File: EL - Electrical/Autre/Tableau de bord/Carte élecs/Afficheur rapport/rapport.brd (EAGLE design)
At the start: 54.9 x 40.9 mm, 15 parts, among them IC1 MCP23008P, X1 22-23-2041

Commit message: Afficheur rapport maj
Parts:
- moved R6 16.1 mm to (44.1, 12.7)
- moved R5 12.4 mm to (29.2, 0.32)
- moved R8 7.63 mm to (28.6, 12.7)
- moved R9 7.31 mm to (28.6, 9.84)
- moved R3 2.56 mm to (28.6, 15.2)
- moved R4 2.56 mm to (28.6, 17.8)
- moved R7 1.42 mm to (29.5, 6.99)
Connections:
- net N$8 renamed SCL
- net N$9 renamed SDA
- removed net N$1: IC1.16, R3.2
- removed net N$3: IC1.14, R5.2
- removed net N$4: IC1.13, R6.2
- removed net N$6: IC1.11, R8.2
- removed net N$7: IC1.10, R9.2
- new net GP0: IC1.10, R5.2
- new net GP1: IC1.11
- new net GP2: IC1.12
- new net GP3: IC1.13, R7.2
- new net GP4: IC1.14, R8.2
- new net GP5: IC1.15, R3.2
- new net GP6: IC1.16, R4.2
- net GND: now also LED1.5
- net N$2: now also R9.2; no longer IC1.15, R4.2
- net N$5: now also R6.2; no longer IC1.12, R7.2
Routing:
- net GND: track 53.6 -> 79.6 mm
- net N$11: track 37.9 -> 30.1 mm
- net N$10: track 49.1 -> 42.2 mm
- net N$14: track 11.9 -> 7.60 mm
- net N$12: track 21.3 -> 17.2 mm
- net N$13: track 14.7 -> 10.6 mm
- net N$16: track 19.5 -> 22.2 mm
- net N$3: track 2.36 -> 0.00 mm
- net N$6: track 2.36 -> 0.00 mm
- net N$4: track 2.27 -> 0.00 mm
- net N$7: track 2.27 -> 0.00 mm
- net N$1: track 2.27 -> 0.00 mm
- net N$5: track 2.22 -> 0.00 mm
- net N$2: track 2.22 -> 0.00 mm
- net N$15: track 21.0 -> 19.3 mm

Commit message: carte afficheur rapport et commandes
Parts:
- removed R3, R4, R5, R6, R7, R8, R9: 470, rcl:0204/7
- added RA, RB, RC, RD, RE, RF, RG: 470, rcl:0204/7
- moved R1 12.8 mm to (23.5, 25.7)
- moved C3 11.4 mm to (6.67, 24.1), turned to 90 degrees
- moved X1 10.3 mm to (23.5, 31.4), turned to 180 degrees
- moved C2 9.89 mm to (13.7, 30.2), turned to 90 degrees
- moved R2 7.31 mm to (6.67, 16.2), turned to 90 degrees
- moved IC1 2.86 mm to (15.6, 12.7)
- moved LED1 2.56 mm to (44.1, 19.4)
- moved C1 1.62 mm to (6.67, 6.67), turned to 270 degrees
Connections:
- removed net N$2: R9.2
- removed net N$5: R6.2
- net +5V: now also LED1.5, X1.1; no longer X1.2
- net GND: now also X1.4; no longer LED1.5, X1.1
- net GP0: now also RC.2; no longer R5.2
- net GP1: now also RD.2
- net GP2: now also RE.2
- net GP3: now also RG.2; no longer R7.2
- net GP4: now also RF.2; no longer R8.2
- net GP5: now also RA.2; no longer R3.2
- net GP6: now also RB.2; no longer R4.2
- net N$10: now also RG.1; no longer R9.1
- net N$11: now also RF.1; no longer R8.1
- net N$12: now also RE.1; no longer R7.1
- net N$13: now also RD.1; no longer R6.1
- net N$14: now also RC.1; no longer R5.1
- net N$15: now also RB.1; no longer R4.1
- net N$16: now also RA.1; no longer R3.1
- net SCL: now also X1.2; no longer X1.4
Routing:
- net GND: track 79.6 -> 53.8 mm
- net +5V: track 114.5 -> 99.7 mm
- net N$13: track 10.6 -> 18.3 mm
- net N$10: track 42.2 -> 36.4 mm
- net N$14: track 7.60 -> 12.8 mm
- net N$12: track 17.2 -> 21.7 mm
- net N$16: track 22.2 -> 26.6 mm
- net SCL: track 31.4 -> 27.7 mm
- net SDA: track 29.1 -> 25.7 mm
- net N$15: track 19.3 -> 21.9 mm
- net GP6: track 0.00 -> 2.54 mm
- net GP5: track 0.00 -> 2.54 mm
- net GP4: track 0.00 -> 2.54 mm
- net GP3: track 0.00 -> 2.54 mm
- net GP2: track 0.00 -> 2.54 mm
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- added copper zone on layer 1, net GND
- added copper zone on layer 1, net SDA
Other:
- board size 54.9 x 40.9 mm -> 63.5 x 38.1 mm
- board text added: "Afficheur Rapport Optimus V1.0"
- board text added: "GND SDA SCL +5V"

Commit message: test sublime merge
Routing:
- net +5V: track 99.7 -> 98.4 mm
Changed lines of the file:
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@@
 <wire x1="2.54" y1="0" x2="0" y2="2.54" width="0.1524" layer="20" curve="-90"/>
 <hole x="5.08" y="1.905" drill="0.0762"/>
-<hole x="11.1125" y="35.8775" drill="0.0762"/>
+<hole x="13.6525" y="35.56" drill="0.0762"/>
 <hole x="60.6425" y="2.54" drill="0.0762"/>
 <wire x1="60.96" y1="0" x2="63.5" y2="2.54" width="0.1524" layer="20" curve="90"/>
@@
 <wire x1="56.515" y1="7.62" x2="56.515" y2="35.56" width="0.1524" layer="20"/>
 <wire x1="56.515" y1="35.56" x2="56.515" y2="36.195" width="0.1524" layer="20"/>
+<dimension x1="2.54" y1="0" x2="2.54" y2="38.1" x3="-8.89" y3="19.05" textsize="1.778" layer="48"/>
+<dimension x1="0" y1="35.56" x2="56.515" y2="35.56" x3="28.2575" y3="43.4975" textsize="1.778" layer="48"/>
+<dimension x1="0" y1="2.54" x2="63.5" y2="2.54" x3="31.75" y3="-8.255" textsize="1.778" layer="48"/>
+<dimension x1="60.96" y1="0" x2="60.96" y2="5.08" x3="71.12" y3="2.54" textsize="1.778" layer="48"/>
 </plain>
 <attributes>
@@
 <wire x1="27.305" y1="22.86" x2="28.575" y2="22.86" width="0.1524" layer="16"/>
 <wire x1="28.575" y1="22.86" x2="39.0525" y2="22.86" width="0.1524" layer="16"/>
-<wire x1="44.1325" y1="27.94" x2="39.0525" y2="22.86" width="0.1524" layer="16"/>
+<wire x1="39.0525" y1="22.86" x2="44.1325" y2="27.94" width="0.1524" layer="16"/>
 <wire x1="8.89" y1="10.16" x2="6.6675" y2="12.3825" width="0.1524" layer="16"/>
 <wire x1="39.0525" y1="22.86" x2="44.1325" y2="17.78" width="0.1524" layer="16"/>
-<contactref element="LED1" pad="5"/>
-<contactref element="LED1" pad="8"/>
-<contactref element="LED1" pad="3"/>
 <wire x1="44.1325" y1="17.78" x2="44.1325" y2="11.7475" width="0.1524" layer="16"/>
-<wire x1="44.1325" y1="11.7475" x2="44.1325" y2="4.1675" width="0.1524" layer="16"/>
-<wire x1="44.1325" y1="34.6475" x2="44.1325" y2="27.94" width="0.1524" layer="16"/>
 <wire x1="6.6675" y1="7.9375" x2="7.3025" y2="8.5725" width="0.1524" layer="16"/>
 <wire x1="7.3025" y1="8.5725" x2="8.89" y2="10.16" width="0.1524" layer="16"/>
@@
 <vertex x="25.7175" y="22.86"/>
 </polygon>
-<wire x1="39.0525" y1="4.1675" x2="39.0525" y2="6.7075" width="0.1524" layer="16"/>
-<wire x1="44.1325" y1="4.1675" x2="44.1325" y2="5.4375" width="0.1524" layer="16"/>
-<wire x1="39.0525" y1="6.7075" x2="44.0925" y2="11.7475" width="0.1524" layer="16"/>
+<wire x1="44.0925" y1="11.7475" x2="39.0525" y2="6.7075" width="0.1524" layer="16"/>
 <wire x1="44.0925" y1="11.7475" x2="44.1325" y2="11.7475" width="0.1524" layer="16"/>
 <polygon width="0.1524" layer="16" isolate="0.254">
@@
 <vertex x="44.1325" y="10.4775"/>
 </polygon>
+<contactref element="LED1" pad="5"/>
+<contactref element="LED1" pad="8"/>
+<contactref element="LED1" pad="3"/>
+<wire x1="44.1325" y1="27.94" x2="44.1325" y2="34.6475" width="0.1524" layer="16"/>
+<wire x1="39.0525" y1="6.7075" x2="39.0525" y2="4.1675" width="0.1524" layer="16"/>
+<wire x1="44.0925" y1="11.7475" x2="44.0925" y2="4.2075" width="0.1524" layer="16"/>
+<wire x1="44.0925" y1="4.2075" x2="44.1325" y2="4.1675" width="0.1524" layer="16"/>
 </signal>
 <signal name="SCL">
@@
 <wire x1="16.51" y1="28.8925" x2="13.6525" y2="28.8925" width="0.1524" layer="1"/>
 <wire x1="19.685" y1="25.7175" x2="16.51" y2="28.8925" width="0.1524" layer="1"/>
-<polygon width="0.1524" layer="1" spacing="0.254" isolate="0.254">
+<polygon width="0.1524" layer="1">
+<vertex x="19.05" y="28.8925"/>
 <vertex x="16.51" y="28.8925"/>
-<vertex x="17.78" y="28.8925"/>
-<vertex x="17.145" y="28.2575"/>
-</polygon>
-</signal>
+<vertex x="18.0975" y="27.305"/>
+<vertex x="19.685" y="28.8925"/>
+</polygon>
+</signal>

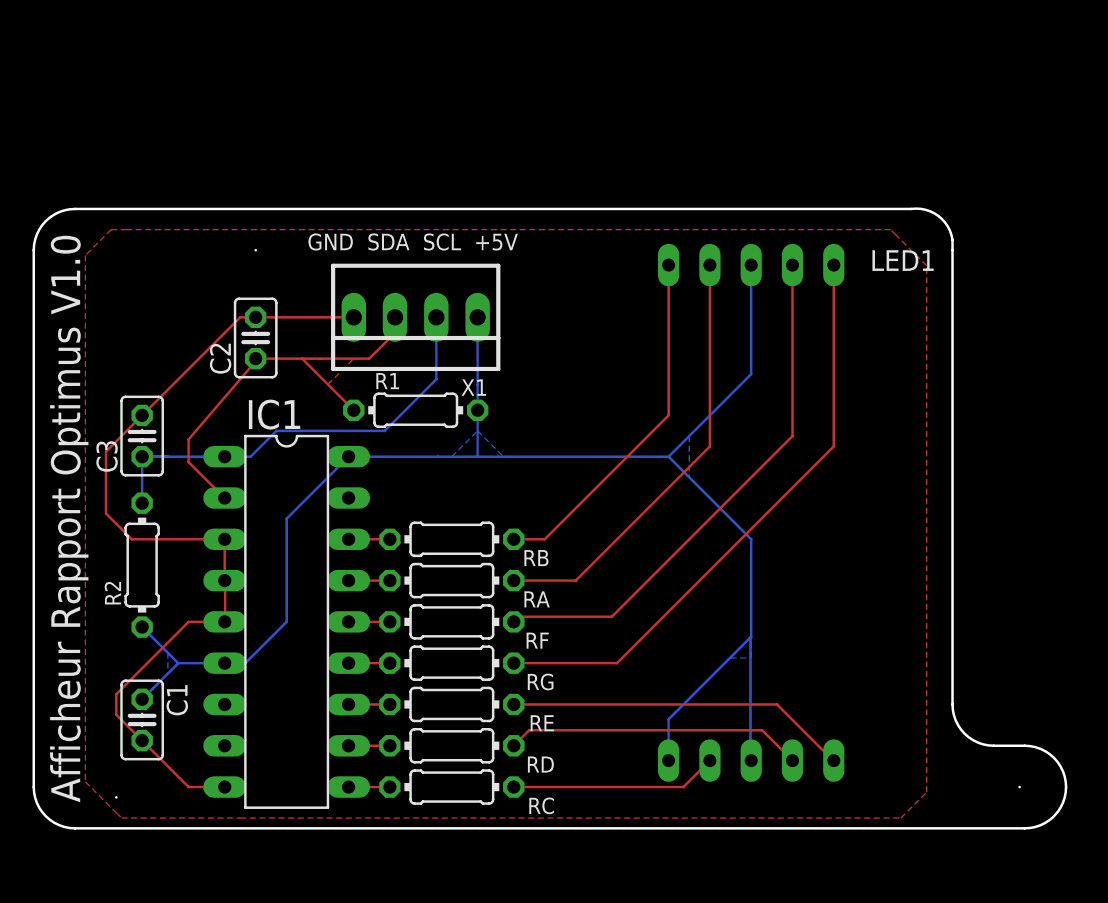
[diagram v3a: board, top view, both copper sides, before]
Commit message: connecteurs Vulcanix et préparation shield carte avant
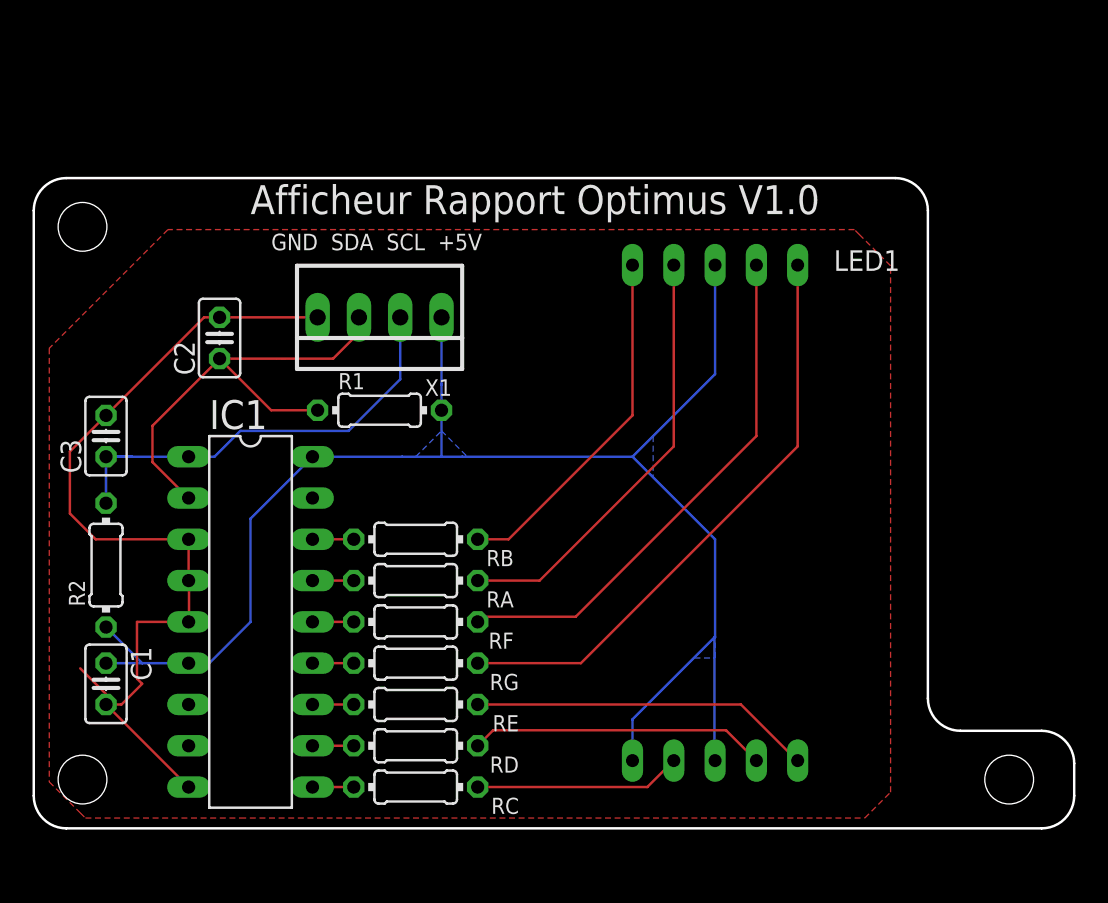
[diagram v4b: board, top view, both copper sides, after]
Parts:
- moved C1 3.14 mm to (4.45, 8.89)
- moved LED1 2.22 mm to (41.9, 19.4)
- moved C2 2.22 mm to (11.4, 30.2)
- moved C3 2.22 mm to (4.45, 24.1)
- moved R1 2.22 mm to (21.3, 25.7)
- moved R2 2.22 mm to (4.45, 16.2)
- moved RA 2.22 mm to (23.5, 15.2)
- moved RB 2.22 mm to (23.5, 17.8)
- moved RC 2.22 mm to (23.5, 2.54)
- moved RD 2.22 mm to (23.5, 5.08)
- moved RE 2.22 mm to (23.5, 7.62)
- moved RF 2.22 mm to (23.5, 12.7)
- moved RG 2.22 mm to (23.5, 10.2)
- moved X1 2.22 mm to (21.3, 31.4)
- moved IC1 2.22 mm to (13.3, 12.7)
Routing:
- net SDA: track 25.7 -> 28.8 mm
- net GND: track 53.8 -> 55.5 mm
- net +5V: track 98.4 -> 97.5 mm
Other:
- board size 63.5 x 38.1 mm -> 64 x 40 mm

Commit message: élec
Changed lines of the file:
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@@
 <?xml version="1.0" encoding="utf-8"?>
 <!DOCTYPE eagle SYSTEM "eagle.dtd">
-<eagle version="9.1.0">
+<eagle version="9.2.1">
 <drawing>
 <settings>
@@
 <layer number="45" name="Holes" color="7" fill="1" visible="yes" active="yes"/>
 <layer number="46" name="Milling" color="3" fill="1" visible="no" active="yes"/>
-<layer number="47" name="Measures" color="7" fill="1" visible="no" active="yes"/>
+<layer number="47" name="Measures" color="7" fill="1" visible="yes" active="yes"/>
 <layer number="48" name="Document" color="7" fill="1" visible="yes" active="yes"/>
 <layer number="49" name="Reference" color="7" fill="1" visible="yes" active="yes"/>
@@
 <dimension x1="0" y1="3" x2="3" y2="3" x3="1.5" y3="-7.21845625" textsize="1.778" layer="48" dtype="diameter"/>
 <dimension x1="3" y1="3" x2="60" y2="3" x3="31.5" y3="-11.483896875" textsize="1.778" layer="48" dtype="diameter"/>
-<dimension x1="53" y1="38" x2="54.73675" y2="38.99181875" x3="61.51006875" y3="42.8599125" textsize="1.778" layer="48" dtype="radius"/>
+<dimension x1="53" y1="38" x2="54.587465625" y2="39.216534375" x3="60.778571875" y3="43.961028125" textsize="1.778" layer="48" dtype="radius"/>
+<dimension x1="48.895" y1="36.21" x2="49.53" y2="40.005" x3="66.675" y3="38.1075" textsize="1.778" layer="47" dtype="vertical"/>
+<dimension x1="53.9" y1="8.89" x2="55" y2="8" x3="54.45" y3="-2.8575" textsize="1.778" layer="47" dtype="horizontal"/>
 </plain>
 <attributes>
@@
 </autorouter>
 <elements>
-<element name="C1" library="rcl" library_urn="urn:adsk.eagle:library:334" package="C025-025X050" package3d_urn="urn:adsk.eagle:package:23629/2" value="500pF" x="4.445" y="8.89" rot="R270">
+<element name="C1" library="rcl" library_urn="urn:adsk.eagle:library:334" package="C025-025X050" package3d_urn="urn:adsk.eagle:package:23629/2" value="500pF" x="4.445" y="8.89" smashed="yes" rot="R270">
+<attribute name="NAME" x="5.969" y="11.176" size="1.27" layer="25" ratio="10" rot="R270"/>
 <attribute name="SPICEPREFIX" value="C" x="4.445" y="8.89" size="1.778" layer="27" rot="R270" display="off"/>
-</element>
-<element name="C2" library="rcl" library_urn="urn:adsk.eagle:library:334" package="C025-025X050" package3d_urn="urn:adsk.eagle:package:23629/2" value="135pF" x="11.43" y="30.1625" rot="R90">
+<attribute name="VALUE" x="1.651" y="11.176" size="1.27" layer="27" ratio="10" rot="R270"/>
+</element>
+<element name="C2" library="rcl" library_urn="urn:adsk.eagle:library:334" package="C025-025X050" package3d_urn="urn:adsk.eagle:package:23629/2" value="135pF" x="11.43" y="30.1625" smashed="yes" rot="R90">
+<attribute name="NAME" x="9.906" y="27.8765" size="1.27" layer="25" ratio="10" rot="R90"/>
 <attribute name="SPICEPREFIX" value="C" x="11.43" y="30.1625" size="1.778" layer="27" rot="R90" display="off"/>
-</element>
-<element name="C3" library="rcl" library_urn="urn:adsk.eagle:library:334" package="C025-025X050" package3d_urn="urn:adsk.eagle:package:23629/2" value="135 pF" x="4.445" y="24.13" rot="R90">
+<attribute name="VALUE" x="14.224" y="27.8765" size="1.27" layer="27" ratio="10" rot="R90"/>
+</element>
+<element name="C3" library="rcl" library_urn="urn:adsk.eagle:library:334" package="C025-025X050" package3d_urn="urn:adsk.eagle:package:23629/2" value="135 pF" x="4.445" y="24.13" smashed="yes" rot="R90">
+<attribute name="NAME" x="2.921" y="21.844" size="1.27" layer="25" ratio="10" rot="R90"/>
 <attribute name="SPICEPREFIX" value="C" x="4.445" y="24.13" size="1.778" layer="27" rot="R90" display="off"/>
-</element>
-<element name="IC1" library="microchip-dspic" package="DIL18" value="MCP23008P" x="13.335" y="12.7" rot="R270"/>
+<attribute name="VALUE" x="7.239" y="21.844" size="1.27" layer="27" ratio="10" rot="R90"/>
+</element>
+<element name="IC1" library="microchip-dspic" package="DIL18" value="MCP23008P" x="13.335" y="12.7" smashed="yes" rot="R270">
+<attribute name="NAME" x="10.795" y="24.5618" size="1.778" layer="25" ratio="10"/>
+<attribute name="VALUE" x="12.446" y="22.86" size="1.778" layer="27" ratio="10" rot="R270"/>
+</element>
 <element name="LED1" library="display-kingbright" library_urn="urn:adsk.eagle:library:213" package="SA10-21" package3d_urn="urn:adsk.eagle:package:13078/1" value="7-SEG_SA10-21" x="41.91" y="19.3675" smashed="yes" rot="MR0">
 <attribute name="MF" value="" x="41.91" y="19.3675" size="1.778" layer="28" rot="MR0" display="off"/>
@@
 <attribute name="VALUE" x="53.0225" y="15.24" size="1.27" layer="27" ratio="10" rot="R90"/>
 </element>
-<element name="R1" library="rcl" library_urn="urn:adsk.eagle:library:334" package="0204/7" package3d_urn="urn:adsk.eagle:package:23498/1" value="1k" x="21.2725" y="25.7175">
+<element name="R1" library="rcl" library_urn="urn:adsk.eagle:library:334" package="0204/7" package3d_urn="urn:adsk.eagle:package:23498/1" value="1k" x="21.2725" y="25.7175" smashed="yes">
+<attribute name="NAME" x="18.7325" y="27.0129" size="0.9906" layer="25" ratio="10"/>
 <attribute name="SPICEPREFIX" value="R" x="21.2725" y="25.7175" size="1.778" layer="27" display="off"/>
-</element>
-<element name="R2" library="rcl" library_urn="urn:adsk.eagle:library:334" package="0204/7" package3d_urn="urn:adsk.eagle:package:23498/1" value="1k" x="4.445" y="16.1925" rot="R90">
+<attribute name="VALUE" x="19.6469" y="25.2349" size="0.9906" layer="27" ratio="10"/>
+</element>
+<element name="R2" library="rcl" library_urn="urn:adsk.eagle:library:334" package="0204/7" package3d_urn="urn:adsk.eagle:package:23498/1" value="1k" x="4.445" y="16.1925" smashed="yes" rot="R90">
+<attribute name="NAME" x="3.1496" y="13.6525" size="0.9906" layer="25" ratio="10" rot="R90"/>
 <attribute name="SPICEPREFIX" value="R" x="4.445" y="16.1925" size="1.778" layer="27" rot="R90" display="off"/>
+<attribute name="VALUE" x="4.9276" y="14.5669" size="0.9906" layer="27" ratio="10" rot="R90"/>
 </element>
 <element name="X1" library="con-molex" library_urn="urn:adsk.eagle:library:165" package="22-23-2041" value="22-23-2041" x="21.2725" y="31.4325" smashed="yes" rot="R180">

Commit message: légère modifs à terminer
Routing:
- net GND: track 55.5 -> 49.9 mm
- net SCL: track 27.7 -> 26.8 mm

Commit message: fin des carte tdb
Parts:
- moved C3 2.54 mm to (4.45, 26.7)
- moved R2 2.54 mm to (4.45, 18.7)
- moved C1 2.22 mm to (4.45, 11.1)
- moved R1 0.32 mm to (21.3, 26.0)
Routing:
- net GND: track 49.9 -> 0.00 mm
- net SDA: track 28.8 -> 24.2 mm
- net N$14: track 12.8 -> 14.2 mm
- net SCL: track 26.8 -> 27.8 mm
- net N$12: track 21.7 -> 21.1 mm
- removed copper zone on layer 16, net +5V
- removed copper zone on layer 1, net SDA

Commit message: afficheur tdb
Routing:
- added copper zone on layer 16, net GND
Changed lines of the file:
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@@
 <setting verticaltext="up"/>
 </settings>
-<grid distance="12.5" unitdist="mil" unit="inch" style="lines" multiple="1" display="no" altdistance="5" altunitdist="mil" altunit="mil"/>
+<grid distance="12.5" unitdist="mil" unit="mm" style="lines" multiple="1" display="no" altdistance="5" altunitdist="mil" altunit="mil"/>
 <layers>
 <layer number="1" name="Top" color="4" fill="1" visible="yes" active="yes"/>
@@
 <wire x1="0" y1="38" x2="2" y2="40" width="0.1524" layer="20" curve="-90"/>
 <wire x1="2" y1="0" x2="0" y2="2" width="0.1524" layer="20" curve="-90"/>
-<hole x="3" y="3" drill="3"/>
-<hole x="3" y="37" drill="3"/>
-<hole x="60" y="3" drill="3"/>
+<hole x="3" y="3" drill="3.05"/>
+<hole x="3" y="37" drill="3.05"/>
+<hole x="60" y="3" drill="3.05"/>
 <wire x1="55" y1="8" x2="55" y2="38" width="0.1524" layer="20"/>
 <wire x1="62" y1="0" x2="64" y2="2" width="0.1524" layer="20" curve="90"/>
@@
 <dimension x1="2" y1="40" x2="2" y2="0" x3="-17.4625" y3="20" textsize="1.778" layer="48"/>
 <dimension x1="0" y1="2" x2="64" y2="2" x3="32" y3="-15.5575" textsize="1.778" layer="48"/>
-<dimension x1="61.5" y1="3.000971875" x2="58.5" y2="2.999028125" x3="59.992484375" y3="14.600875" textsize="1.778" layer="48" dtype="diameter"/>
 <dimension x1="62" y1="0" x2="62" y2="6" x3="74.295" y3="3" textsize="1.778" layer="48"/>
 <dimension x1="3" y1="3" x2="3" y2="37" x3="-12.3825" y3="20" textsize="1.778" layer="48"/>
@@
 <dimension x1="48.895" y1="36.21" x2="49.53" y2="40.005" x3="66.675" y3="38.1075" textsize="1.778" layer="47" dtype="vertical"/>
 <dimension x1="53.9" y1="8.89" x2="55" y2="8" x3="54.45" y3="-2.8575" textsize="1.778" layer="47" dtype="horizontal"/>
+<dimension x1="58.475" y1="3.002053125" x2="61.525" y2="2.997946875" x3="60.007503125" y3="8.5725" textsize="1.778" layer="47" dtype="diameter"/>
 </plain>
 <attributes>
@@
 <vertex x="0.9525" y="28.575"/>
 </polygon>
+<polygon width="0.1524" layer="16">
+<vertex x="1.5875" y="7.9375"/>
+<vertex x="0.9525" y="8.5725"/>
+<vertex x="0.9525" y="28.575"/>
+<vertex x="10.4775" y="38.1"/>
+<vertex x="48.895" y="38.1"/>
+<vertex x="51.7525" y="35.2425"/>
+<vertex x="51.7525" y="3.4925"/>
+<vertex x="49.2125" y="0.9525"/>
+<vertex x="8.255" y="0.9525"/>
+<vertex x="7.3025" y="1.905"/>
+<vertex x="7.3025" y="6.6675"/>
+<vertex x="7.3025" y="7.3025"/>
+<vertex x="6.6675" y="7.9375"/>
+</polygon>
 </signal>
 <signal name="+5V">
@@
 <contactref element="LED1" pad="9"/>
 <contactref element="RF" pad="1"/>
-<wire x1="27.305" y1="12.7" x2="27.6225" y2="13.0175" width="0.1524" layer="1"/>
-<wire x1="27.6225" y1="13.0175" x2="33.3375" y2="13.0175" width="0.6096" layer="1"/>
-<wire x1="33.3375" y1="13.0175" x2="44.45" y2="24.13" width="0.6096" layer="1"/>
+<wire x1="44.45" y1="24.13" x2="33.3375" y2="13.0175" width="0.6096" layer="1"/>
 <wire x1="44.45" y1="24.13" x2="44.45" y2="34.6475" width="0.6096" layer="1"/>
+<wire x1="33.3375" y1="13.0175" x2="33.02" y2="12.7" width="0.6096" layer="1"/>
+<wire x1="33.02" y1="12.7" x2="27.305" y2="12.7" width="0.6096" layer="1"/>
 </signal>
 <signal name="N$12">
